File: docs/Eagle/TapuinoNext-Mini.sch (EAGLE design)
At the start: 10 parts, among them U1 ESP32-DEVKITC-38

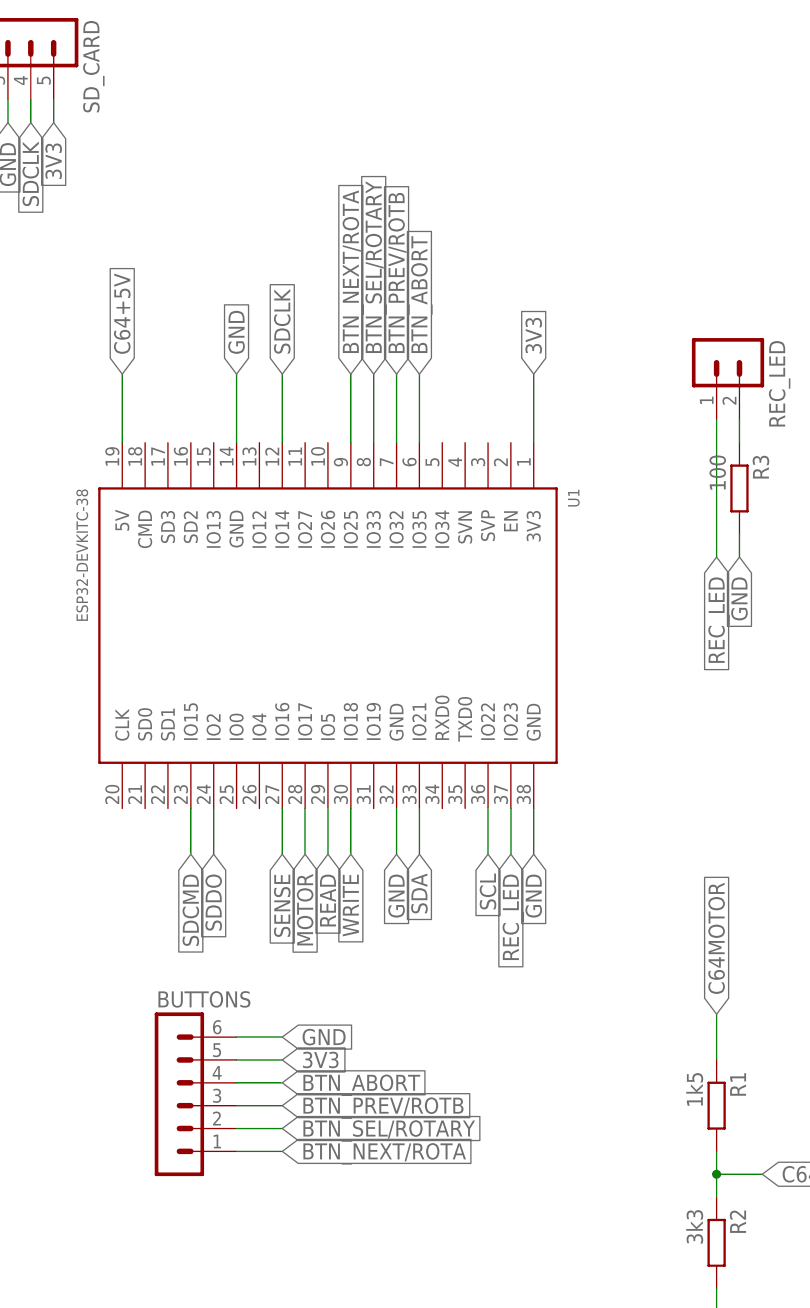
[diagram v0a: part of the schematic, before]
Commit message: Changed rotary wiring back to original to match stripboard
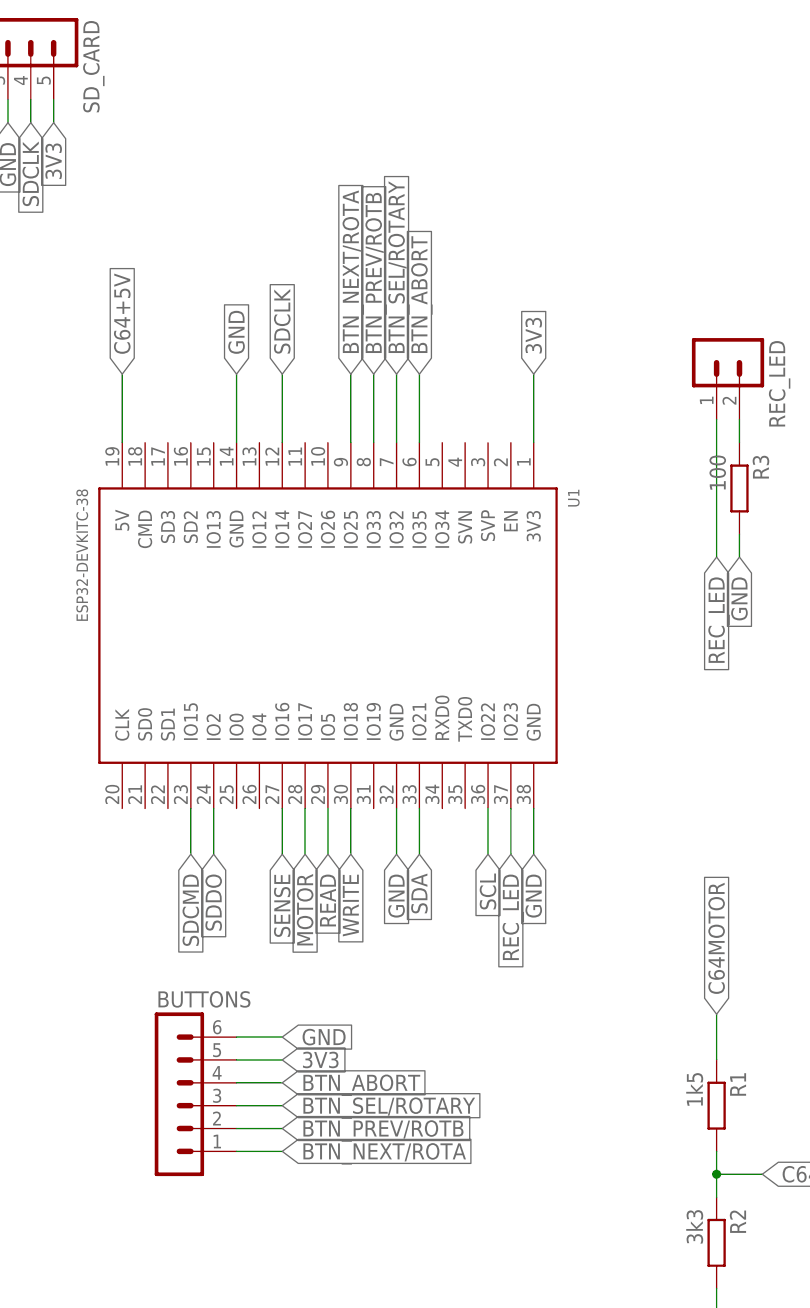
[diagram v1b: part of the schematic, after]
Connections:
- net BTN_PREV/ROTB: now also BUTTONS.2, U1.IO33; no longer BUTTONS.3, U1.IO32
- net BTN_SEL/ROTARY: now also BUTTONS.3, U1.IO32; no longer BUTTONS.2, U1.IO33
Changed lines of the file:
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@@
 <net name="BTN_PREV/ROTB" class="0">
 <segment>
+<pinref part="U1" gate="G$1" pin="IO33"/>
+<wire x1="50.8" y1="66.04" x2="50.8" y2="73.66" width="0.1524" layer="91"/>
+<label x="50.8" y="73.66" size="1.778" layer="95" rot="R90" xref="yes"/>
+</segment>
+<segment>
+<pinref part="BUTTONS" gate="1" pin="2"/>
+<wire x1="35.56" y1="-10.16" x2="40.64" y2="-10.16" width="0.1524" layer="91"/>
+<label x="40.64" y="-10.16" size="1.778" layer="95" xref="yes"/>
+</segment>
+</net>
+<net name="BTN_SEL/ROTARY" class="0">
+<segment>
+<pinref part="U1" gate="G$1" pin="IO32"/>
 <wire x1="53.34" y1="66.04" x2="53.34" y2="73.66" width="0.1524" layer="91"/>
 <label x="53.34" y="73.66" size="1.778" layer="95" rot="R90" xref="yes"/>
-<pinref part="U1" gate="G$1" pin="IO32"/>
 </segment>
 <segment>
@@
 </segment>
 </net>
-<net name="BTN_SEL/ROTARY" class="0">
-<segment>
-<wire x1="50.8" y1="66.04" x2="50.8" y2="73.66" width="0.1524" layer="91"/>
-<label x="50.8" y="73.66" size="1.778" layer="95" rot="R90" xref="yes"/>
-<pinref part="U1" gate="G$1" pin="IO33"/>
-</segment>
-<segment>
-<pinref part="BUTTONS" gate="1" pin="2"/>
-<wire x1="35.56" y1="-10.16" x2="40.64" y2="-10.16" width="0.1524" layer="91"/>
-<label x="40.64" y="-10.16" size="1.778" layer="95" xref="yes"/>
-</segment>
-</net>

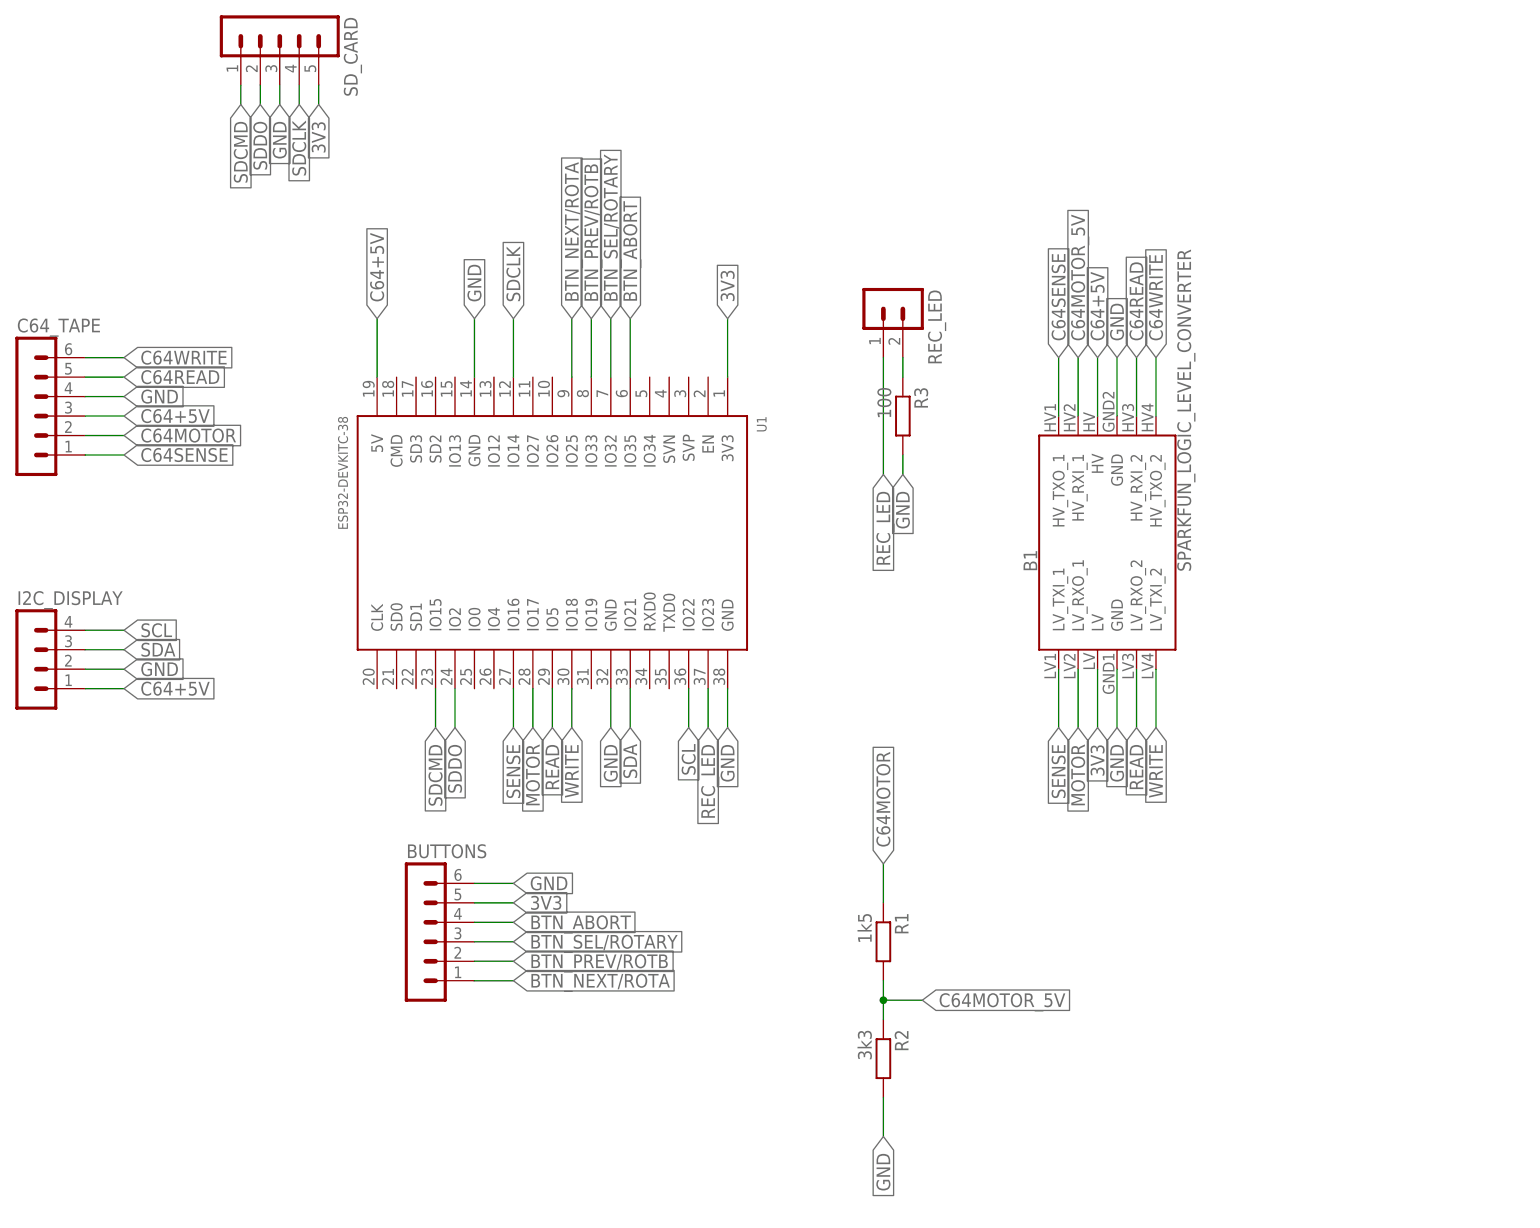
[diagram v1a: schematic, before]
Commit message: Fixed pinout across all of the schematics, hopefully for the last time
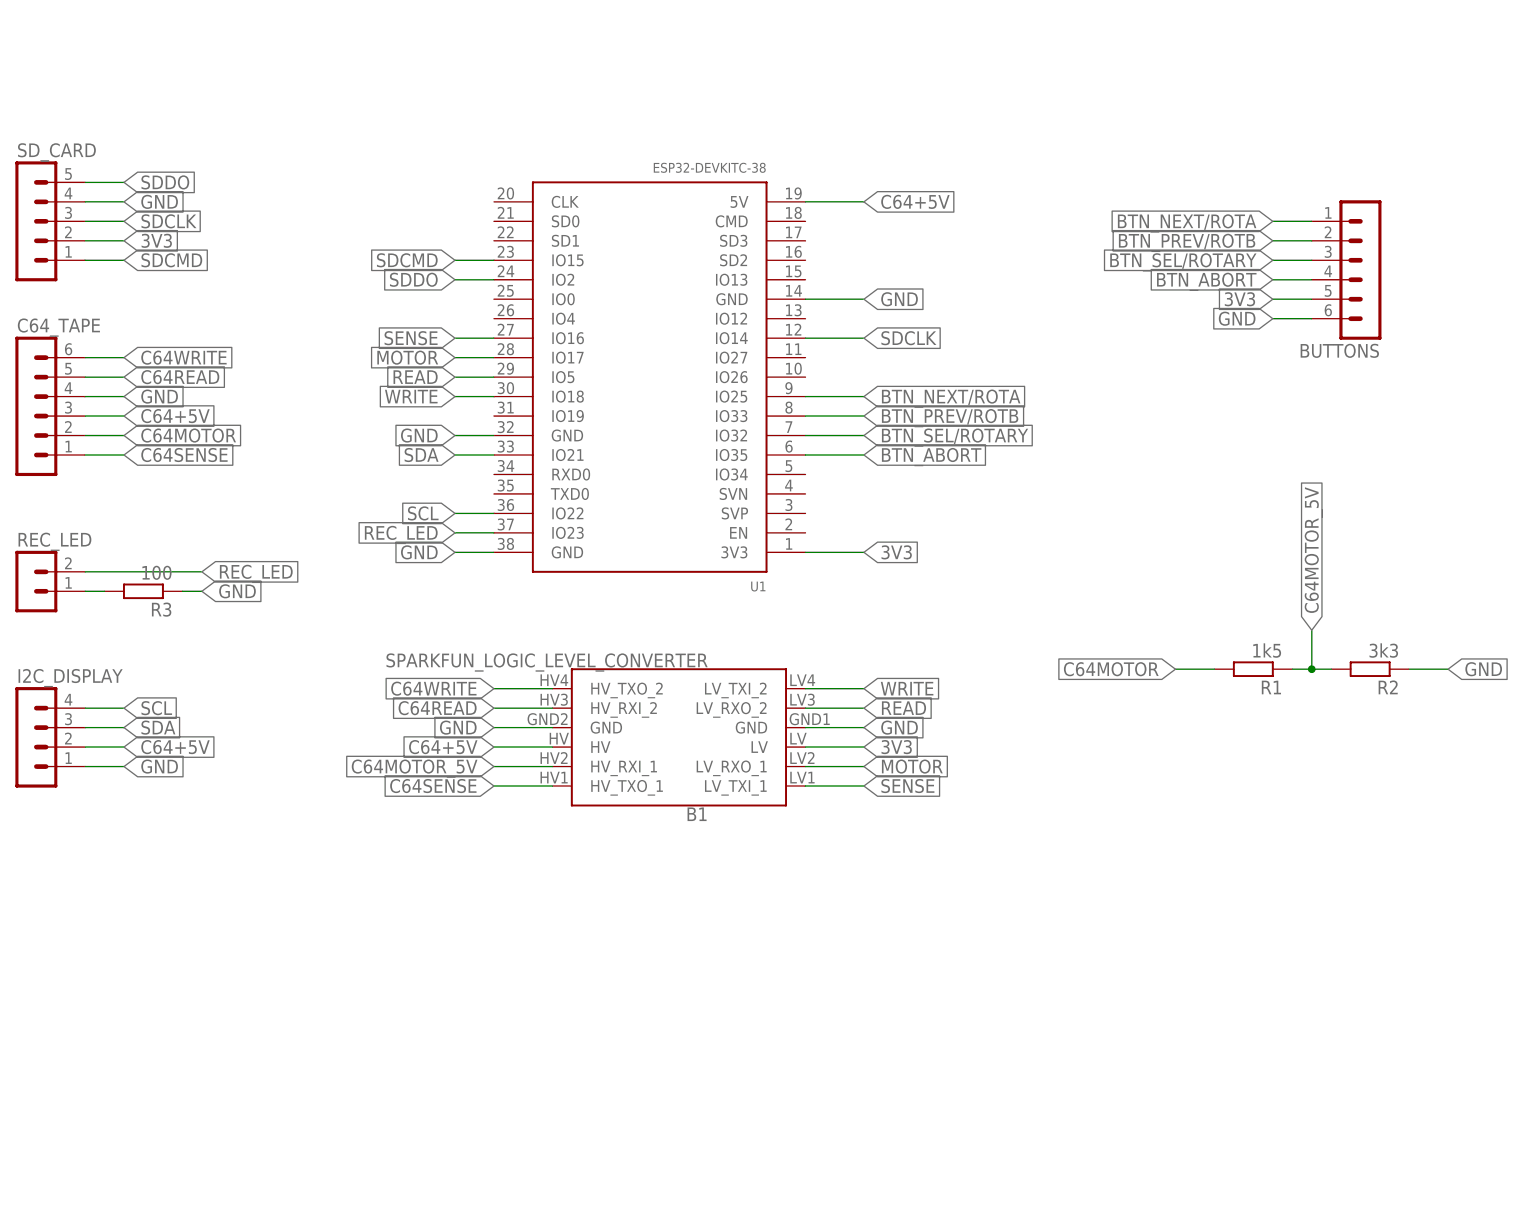
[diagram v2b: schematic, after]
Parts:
- R1, R2, R3: device rcl:R-EU_0204/7 -> rcl:R-EU_0207/10
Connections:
- removed net N$2: R3.1, REC_LED.2
- new net N$1: R3.2, REC_LED.1
- net 3V3: now also SD_CARD.2; no longer SD_CARD.5
- net C64+5V: now also I2C_DISPLAY.2; no longer I2C_DISPLAY.1
- net C64MOTOR: now also R1.2; no longer R1.1
- net C64MOTOR_5V: now also R1.1, R2.2; no longer R1.2, R2.1
- net GND: now also I2C_DISPLAY.1, R2.1, R3.1, SD_CARD.4; no longer I2C_DISPLAY.2, R2.2, R3.2, SD_CARD.3
- net REC_LED: now also REC_LED.2; no longer REC_LED.1
- net SDCLK: now also SD_CARD.3; no longer SD_CARD.4
- net SDDO: now also SD_CARD.5; no longer SD_CARD.2
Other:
- moved on the sheet: B1, BUTTONS, I2C_DISPLAY, R1, R2, R3, REC_LED, SD_CARD, U1
